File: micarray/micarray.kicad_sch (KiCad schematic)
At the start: 37 parts, among them IC1 74LCX125MTCX, J1 Previous, J2 Next, J3 MCHStreamer J3

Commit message: save
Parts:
- J1: footprint Connector_PinSocket_2.54mm:PinSocket_1x09_P2.54mm_Horizontal -> Connector_PinSocket_2.54mm:PinSocket_2x05_P2.54mm_Horizontal
- J2: footprint Connector_PinHeader_2.54mm:PinHeader_1x09_P2.54mm_Horizontal -> Connector_PinHeader_2.54mm:PinHeader_2x05_P2.54mm_Horizontal
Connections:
- net PDM_DATA2: now also J1.1 (Pin_1); no longer J1.6 (Pin_6)
- net PDM_DATA3: now also J1.2 (Pin_2); no longer J1.5 (Pin_5)
- net PDM_DATA4: now also J1.3 (Pin_3); no longer J1.4 (Pin_4)
- net PDM_DATA5: now also J1.4 (Pin_4); no longer J1.3 (Pin_3)
- net PDM_DATA6: now also J1.5 (Pin_5); no longer J1.2 (Pin_2)
- net PDM_DATA7: now also J1.6 (Pin_6); no longer J1.1 (Pin_1)
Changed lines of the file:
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@@
 		)
 	)
-	(global_label "PDM_DATA5"
-		(shape input)
-		(at 292.1 50.8 180)
-		(fields_autoplaced yes)
-		(effects
-			(font
-				(size 1.27 1.27)
-			)
-			(justify right)
-		)
-		(property "Intersheetrefs" "${INTERSHEET_REFS}"
-			(at 278.5315 50.8 0)
-			(effects
-				(font
-					(size 1.27 1.27)
-				)
-				(justify right)
-				(hide yes)
-			)
-		)
-	)
-	(global_label "PDM_DATA2"
-		(shape input)
-		(at 292.1 58.42 180)
-		(fields_autoplaced yes)
-		(effects
-			(font
-				(size 1.27 1.27)
-			)
-			(justify right)
-		)
-		(property "Intersheetrefs" "${INTERSHEET_REFS}"
-			(at 278.5315 58.42 0)
-			(effects
-				(font
-					(size 1.27 1.27)
-				)
-				(justify right)
-				(hide yes)
-			)
-		)
-	)
 	(global_label "PDM_CLK-IN"
 		(shape input)
@@
 		)
 	)
-	(global_label "PDM_DATA3"
+	(global_label "PDM_DATA0"
 		(shape input)
-		(at 292.1 55.88 180)
+		(at 215.9 62.23 180)
 		(fields_autoplaced yes)
 		(effects
@@
 		)
 		(property "Intersheetrefs" "${INTERSHEET_REFS}"
-			(at 278.5315 55.88 0)
+			(at 202.3315 62.23 0)
 			(effects
 				(font
@@
 		)
 	)
-	(global_label "PDM_DATA0"
+	(global_label "PDM_DATA3"
 		(shape input)
-		(at 215.9 62.23 180)
+		(at 292.1 48.26 180)
 		(fields_autoplaced yes)
 		(effects
@@
 		)
 		(property "Intersheetrefs" "${INTERSHEET_REFS}"
-			(at 202.3315 62.23 0)
+			(at 278.5315 48.26 0)
 			(effects
 				(font
@@
 		)
 	)
+	(global_label "PDM_CLK0"
+		(shape input)
+		(at 347.98 53.34 180)
+		(fields_autoplaced yes)
+		(effects
+			(font
+				(size 1.27 1.27)
+			)
+			(justify right)
+		)
+		(property "Intersheetrefs" "${INTERSHEET_REFS}"
+			(at 335.2582 53.34 0)
+			(effects
+				(font
+					(size 1.27 1.27)
+				)
+				(justify right)
+				(hide yes)
+			)
+		)
+	)
 	(global_label "PDM_DATA6"
 		(shape input)
-		(at 292.1 48.26 180)
+		(at 292.1 55.88 180)
 		(fields_autoplaced yes)
 		(effects
@@
 		)
 		(property "Intersheetrefs" "${INTERSHEET_REFS}"
-			(at 278.5315 48.26 0)
+			(at 278.5315 55.88 0)
 			(effects
 				(font
@@
 		)
 	)
-	(global_label "PDM_CLK0"
+	(global_label "PDM_DATA7"
 		(shape input)
-		(at 347.98 53.34 180)
+		(at 292.1 58.42 180)
 		(fields_autoplaced yes)
 		(effects
@@
 		)
 		(property "Intersheetrefs" "${INTERSHEET_REFS}"
-			(at 335.2582 53.34 0)
+			(at 278.5315 58.42 0)
 			(effects
 				(font
@@
 		)
 	)
+	(global_label "PDM_DATA5"
+		(shape input)
+		(at 292.1 53.34 180)
+		(fields_autoplaced yes)
+		(effects
+			(font
+				(size 1.27 1.27)
+			)
+			(justify right)
+		)
+		(property "Intersheetrefs" "${INTERSHEET_REFS}"
+			(at 278.5315 53.34 0)
+			(effects
+				(font
+					(size 1.27 1.27)
+				)
+				(justify right)
+				(hide yes)
+			)
+		)
+	)
 	(global_label "PDM_DATA4"
 		(shape input)
@@
 	(global_label "PDM_DATA4"
 		(shape input)
-		(at 292.1 53.34 180)
+		(at 292.1 50.8 180)
 		(fields_autoplaced yes)
 		(effects
@@
 		)
 		(property "Intersheetrefs" "${INTERSHEET_REFS}"
-			(at 278.5315 53.34 0)
+			(at 278.5315 50.8 0)
 			(effects
 				(font
@@
 		)
 	)
-	(global_label "PDM_DATA7"
+	(global_label "PDM_DATA2"
 		(shape input)
 		(at 292.1 45.72 180)
@@
 			)
 		)
-		(property "Footprint" "Connector_PinSocket_2.54mm:PinSocket_1x09_P2.54mm_Horizontal"
+		(property "Footprint" "Connector_PinSocket_2.54mm:PinSocket_2x05_P2.54mm_Horizontal"
 			(at 297.18 55.88 0)
 			(effects
@@
 			)
 		)
-		(property "Footprint" "Connector_PinHeader_2.54mm:PinHeader_1x09_P2.54mm_Horizontal"
+		(property "Footprint" "Connector_PinHeader_2.54mm:PinHeader_2x05_P2.54mm_Horizontal"
 			(at 297.18 81.28 0)
 			(effects

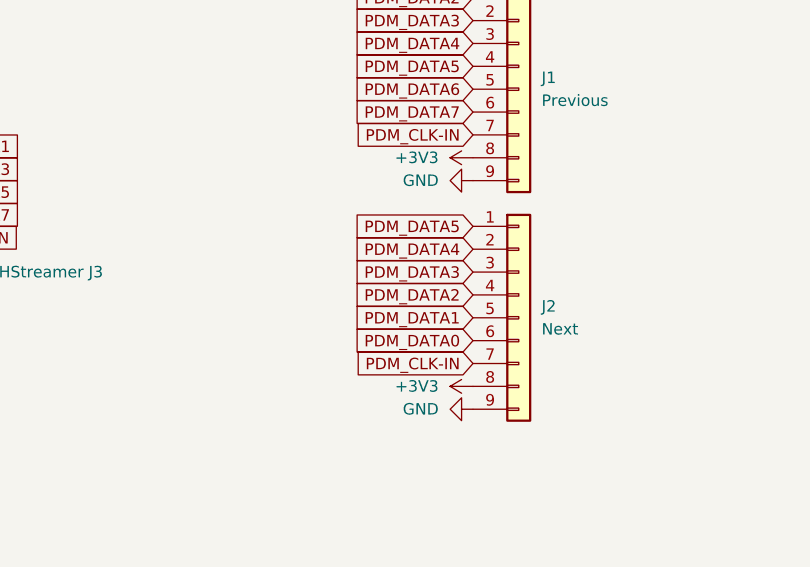
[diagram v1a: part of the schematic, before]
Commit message: All traces, no ground to mic
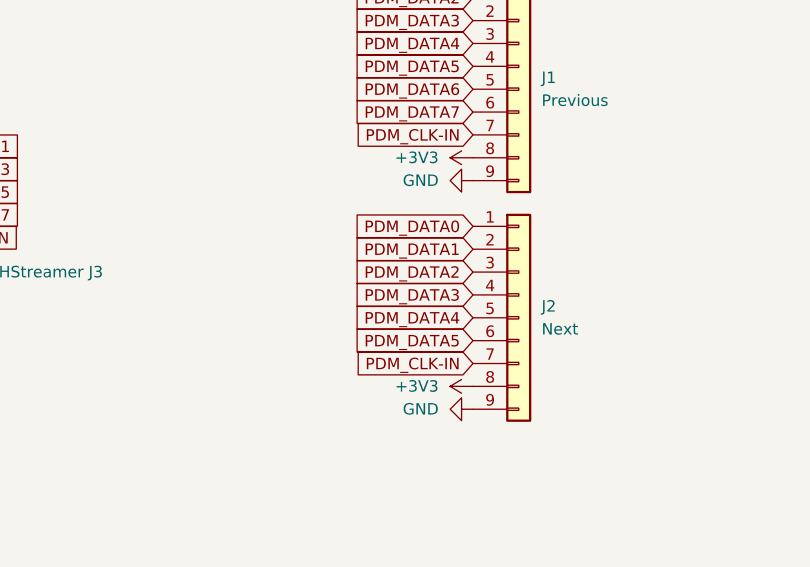
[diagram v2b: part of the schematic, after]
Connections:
- net PDM_DATA0: now also J2.1 (Pin_1); no longer J2.6 (Pin_6)
- net PDM_DATA1: now also J2.2 (Pin_2); no longer J2.5 (Pin_5)
- net PDM_DATA2: now also J2.3 (Pin_3); no longer J2.4 (Pin_4)
- net PDM_DATA3: now also J2.4 (Pin_4); no longer J2.3 (Pin_3)
- net PDM_DATA4: now also J2.5 (Pin_5); no longer J2.2 (Pin_2)
- net PDM_DATA5: now also J2.6 (Pin_6); no longer J2.1 (Pin_1)

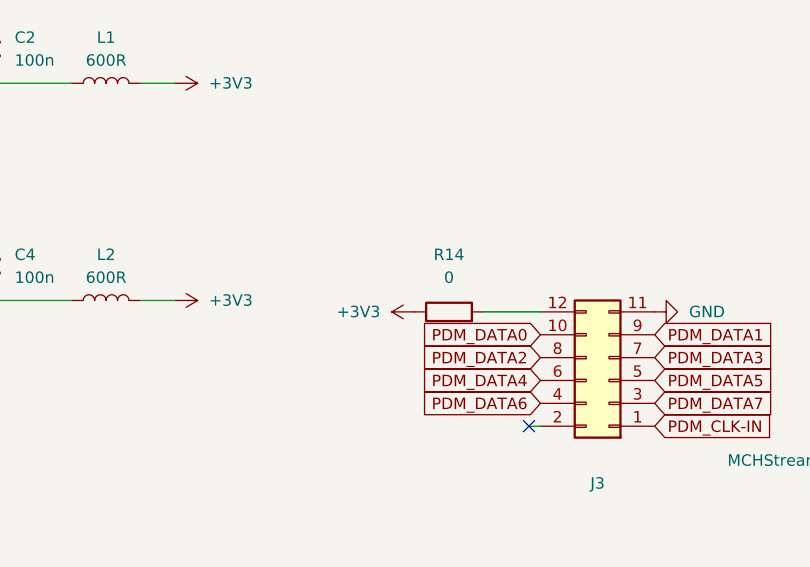
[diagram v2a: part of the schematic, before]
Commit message: JLC IDs added, pre TSSOP14
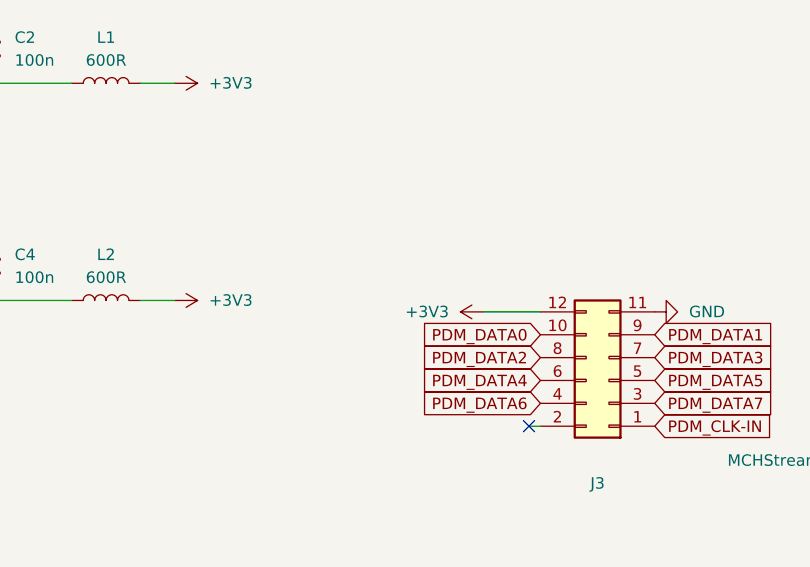
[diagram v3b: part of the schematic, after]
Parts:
- removed R14: 0, Resistor_SMD:R_0603_1608Metric_Pad0.98x0.95mm_HandSolder, symbol Device:R
- C1, C3, C5, C7, C9: LCSC Part # (none) -> C126538
- C10, C2, C4, C6, C8: LCSC Part # (none) -> C77014
- IC1: LCSC Part # (none) -> C141450
- J1: LCSC Part # (none) -> C5142480
- J2: LCSC Part # (none) -> C60563
- J3: LCSC Part # (none) -> C60565
- L1, L2, L3, L4, L5: LCSC Part # (none) -> C2971884
- MK1, MK2, MK3, MK4: LCSC Part # (none) -> C3040249
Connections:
- net +3V3: now also J3.12 (Pin_12)

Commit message: Change Mic and IC footprint
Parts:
- C1, C3, C5, C7, C9: LCSC Part # C126538 -> C71653
- C10, C2, C4, C6, C8: LCSC Part # C77014 -> C77055
- IC1: footprint Package_SO:TSSOP-14_4.4x3.6mm_P0.4mm -> Package_SO:TSSOP-14_4.4x5mm_P0.65mm
- MK1, MK2, MK3, MK4: footprint SPH1668LM4H_1:MIC_SPH1668LM4H-1 -> Sensor_Audio:Knowles_LGA-5_3.5x2.65mm
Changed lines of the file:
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@@
 			)
 		)
-		(property "LCSC Part #" "C77014"
+		(property "LCSC Part #" "C77055"
 			(at 153.67 119.38 0)
 			(effects
@@
 			)
 		)
-		(property "LCSC Part #" "C77014"
+		(property "LCSC Part #" "C77055"
 			(at 153.67 95.25 0)
 			(effects
@@
 			)
 		)
-		(property "LCSC Part #" "C126538"
+		(property "LCSC Part #" "C71653"
 			(at 139.7 30.48 0)
 			(effects
@@
 			)
 		)
-		(property "LCSC Part #" "C126538"
+		(property "LCSC Part #" "C71653"
 			(at 422.91 36.83 0)
 			(effects
@@
 			)
 		)
-		(property "Footprint" "SPH1668LM4H_1:MIC_SPH1668LM4H-1"
+		(property "Footprint" "Sensor_Audio:Knowles_LGA-5_3.5x2.65mm"
 			(at 85.09 128.27 0)
 			(effects
@@
 			)
 		)
-		(property "LCSC Part #" "C77014"
+		(property "LCSC Part #" "C77055"
 			(at 153.67 30.48 0)
 			(effects
@@
 			)
 		)
-		(property "LCSC Part #" "C126538"
+		(property "LCSC Part #" "C71653"
 			(at 139.7 95.25 0)
 			(effects
@@
 			)
 		)
-		(property "LCSC Part #" "C77014"
+		(property "LCSC Part #" "C77055"
 			(at 436.88 36.83 0)
 			(effects
@@
 			)
 		)
-		(property "Footprint" "Package_SO:TSSOP-14_4.4x3.6mm_P0.4mm"
+		(property "Footprint" "Package_SO:TSSOP-14_4.4x5mm_P0.65mm"
 			(at 394.97 38.1 0)
 			(effects
@@
 			)
 		)
-		(property "LCSC Part #" "C126538"
+		(property "LCSC Part #" "C71653"
 			(at 139.7 54.61 0)
 			(effects
@@
 			)
 		)
-		(property "Footprint" "SPH1668LM4H_1:MIC_SPH1668LM4H-1"
+		(property "Footprint" "Sensor_Audio:Knowles_LGA-5_3.5x2.65mm"
 			(at 85.09 39.37 0)
 			(effects
@@
 			)
 		)
-		(property "LCSC Part #" "C126538"
+		(property "LCSC Part #" "C71653"
 			(at 139.7 119.38 0)
 			(effects
@@
 			)
 		)
-		(property "Footprint" "SPH1668LM4H_1:MIC_SPH1668LM4H-1"
+		(property "Footprint" "Sensor_Audio:Knowles_LGA-5_3.5x2.65mm"
 			(at 85.09 63.5 0)
 			(effects
@@
 			)
 		)
-		(property "LCSC Part #" "C77014"
+		(property "LCSC Part #" "C77055"
 			(at 153.67 54.61 0)
 			(effects
@@
 			)
 		)
-		(property "Footprint" "SPH1668LM4H_1:MIC_SPH1668LM4H-1"
+		(property "Footprint" "Sensor_Audio:Knowles_LGA-5_3.5x2.65mm"
 			(at 85.09 104.14 0)
 			(effects

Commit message: mounting hole
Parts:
- added C11: 20p, Capacitor_SMD:C_0603_1608Metric_Pad1.08x0.95mm_HandSolder, symbol Device:C
- J3: footprint Connector_PinHeader_2.54mm:PinHeader_2x06_P2.54mm_Horizontal -> Connector_PinHeader_2.54mm:PinHeader_2x06_P2.54mm_Vertical
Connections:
- net +3V3: now also C11.1
- net GND: now also MK1.2 (SELECT), MK3.2 (SELECT), C11.2; no longer MK2.2 (SELECT), MK4.2 (SELECT)
- net at C7.2, C8.2, L4.1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: now also MK4.2 (SELECT)
- net at C5.2, C6.2, L3.1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: no longer MK3.2 (SELECT)
- net at C1.2, C2.2, L1.1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: no longer MK1.2 (SELECT)
- net at C3.2, C4.2, L2.1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: now also MK2.2 (SELECT)

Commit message: 8ch progress, new mics for 16ch
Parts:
- removed MK1, MK2, MK3, MK4: SPH1668LM4H-1, Sensor_Audio:Knowles_LGA-5_3.5x2.65mm, symbol SPH1668LM4H-1:SPH1668LM4H-1
- added MK1, MK2, MK3, MK4: IM73D122V01XTMA1, ProLibrary_pcs_2024-08-08:MIC-SMD_5P-L4.0-W3.0-P0.70-TR_IM69D130V01, symbol 2024-08-08_08-44-14:IM73D122V01XTMA1
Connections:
- net GND: now also MK1.4 (LR), MK1.5 (GND), MK2.5 (GND), MK3.4 (LR), MK3.5 (GND), MK4.5 (GND)
- net at C7.2, C8.2, L4.1: now also MK4.2 (VDD), MK4.4 (LR)
- net at C5.2, C6.2, L3.1: now also MK3.2 (VDD)
- net at C1.2, C2.2, L1.1: now also MK1.2 (VDD)
- net at R8.1: now also MK4.1 (DATA)
- net at R7.2: now also MK4.3 (CLOCK)
- net at R4.1: now also MK2.1 (DATA)
- net at C3.2, C4.2, L2.1: now also MK2.2 (VDD), MK2.4 (LR)
- net at R3.2: now also MK2.3 (CLOCK)
- net at R1.2: now also MK1.3 (CLOCK)
- net at R2.1: now also MK1.1 (DATA)
- net at R5.2: now also MK3.3 (CLOCK)
- net at R6.1: now also MK3.1 (DATA)
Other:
- moved on the sheet: R1, R3, R5, R7

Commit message: 16ch V2 ordered
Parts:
- C11: LCSC Part # C71653 -> C126554
- J3: footprint Connector_PinHeader_2.54mm:PinHeader_2x06_P2.54mm_Vertical -> Connector_PinHeader_2.00mm:PinHeader_2x06_P2.00mm_Vertical; LCSC Part # C60565 -> C225291
- MK1, MK2, MK3, MK4: footprint ProLibrary_pcs_2024-08-08:MIC-SMD_5P-L4.0-W3.0-P0.70-TR_IM69D130V01 -> ul_IM73D122V01XTMA1:PG-LLGA-5-2_INF; LCSC Part # (none) -> C5563886
- R1, R10, R11, R12, R13, R2, R3, R4, R5, R6, R7, R8, R9: LCSC Part # (none) -> C23140

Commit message: Clock line capacitor was in the wrong place
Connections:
- net +3V3: no longer C11.1
- net PDM_CLK-IN: now also C11.1
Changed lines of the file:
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@@
 	)
 	(junction
-		(at 215.9 59.69)
-		(diameter 0)
-		(color 0 0 0 0)
-	)
-	(junction
 		(at 153.67 58.42)
 		(diameter 0)
@@
 	)
 	(junction
-		(at 228.6 59.69)
-		(diameter 0)
-		(color 0 0 0 0)
-	)
-	(junction
 		(at 364.49 43.18)
 		(diameter 0)
@@
 	(wire
 		(pts
-			(xy 215.9 54.61) (xy 215.9 59.69)
-		)
-		(stroke
-			(width 0)
-			(type default)
-		)
-	)
-	(wire
-		(pts
 			(xy 416.56 48.26) (xy 420.37 48.26)
 		)
@@
 	(wire
 		(pts
-			(xy 226.06 54.61) (xy 228.6 54.61)
-		)
-		(stroke
-			(width 0)
-			(type default)
-		)
-	)
-	(wire
-		(pts
 			(xy 100.33 101.6) (xy 139.7 101.6)
 		)
@@
 	(wire
 		(pts
-			(xy 228.6 54.61) (xy 228.6 59.69)
-		)
-		(stroke
-			(width 0)
-			(type default)
-		)
-	)
-	(wire
-		(pts
 			(xy 139.7 125.73) (xy 139.7 123.19)
 		)
@@
 	(wire
 		(pts
-			(xy 218.44 54.61) (xy 215.9 54.61)
-		)
-		(stroke
-			(width 0)
-			(type default)
-		)
-	)
-	(wire
-		(pts
 			(xy 398.78 48.26) (xy 408.94 48.26)
 		)
@@
 		)
 	)
+	(global_label "PDM_CLK-IN"
+		(shape input)
+		(at 218.44 54.61 180)
+		(fields_autoplaced yes)
+		(effects
+			(font
+				(size 1.27 1.27)
+			)
+			(justify right)
+		)
+		(property "Intersheetrefs" "${INTERSHEET_REFS}"
+			(at 203.42 54.61 0)
+			(effects
+				(font
+					(size 1.27 1.27)
+				)
+				(justify right)
+				(hide yes)
+			)
+		)
+	)
 	(global_label "PDM_CLK2"
 		(shape input)
@@
 					(unit 1)
 				)
+			)
+		)
+	)
+	(symbol
+		(lib_id "power:GND")
+		(at 226.06 54.61 90)
+		(unit 1)
+		(exclude_from_sim no)
+		(in_bom yes)
+		(on_board yes)
+		(dnp no)
+		(property "Reference" "#PWR014"
+			(at 232.41 54.61 0)
+			(effects
+				(font
+					(size 1.27 1.27)
+				)
+				(hide yes)
+			)
+		)
+		(property "Value" "GND"
+			(at 229.87 54.6099 90)
+			(effects
+				(font
+					(size 1.27 1.27)
+				)
+				(justify right)
+			)
+		)
+		(property "Footprint" ""
+			(at 226.06 54.61 0)
+			(effects
+				(font
+					(size 1.27 1.27)
+				)
+				(hide yes)
+			)
+		)
+		(property "Datasheet" ""
+			(at 226.06 54.61 0)
+			(effects
+				(font
+					(size 1.27 1.27)
+				)
+				(hide yes)
+			)
+		)
+		(property "Description" "Power symbol creates a global label with name \"GND\" , ground"
+			(at 226.06 54.61 0)
+			(effects
+				(font
+					(size 1.27 1.27)
+				)
+				(hide yes)
+			)
+		)
+		(pin "1"
+		)
+		(instances
+			(project "micarray"
+				(path "/eb6ae12f-c88f-4fc4-8e17-c302a27a2d54"
+					(reference "#PWR014")
+					(unit 1)
+				)
